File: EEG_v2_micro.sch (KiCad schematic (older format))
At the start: 19 parts, among them U6 CC2540, U7 2450BM15A0002E, X1 32-MHz, X2 32-MHz

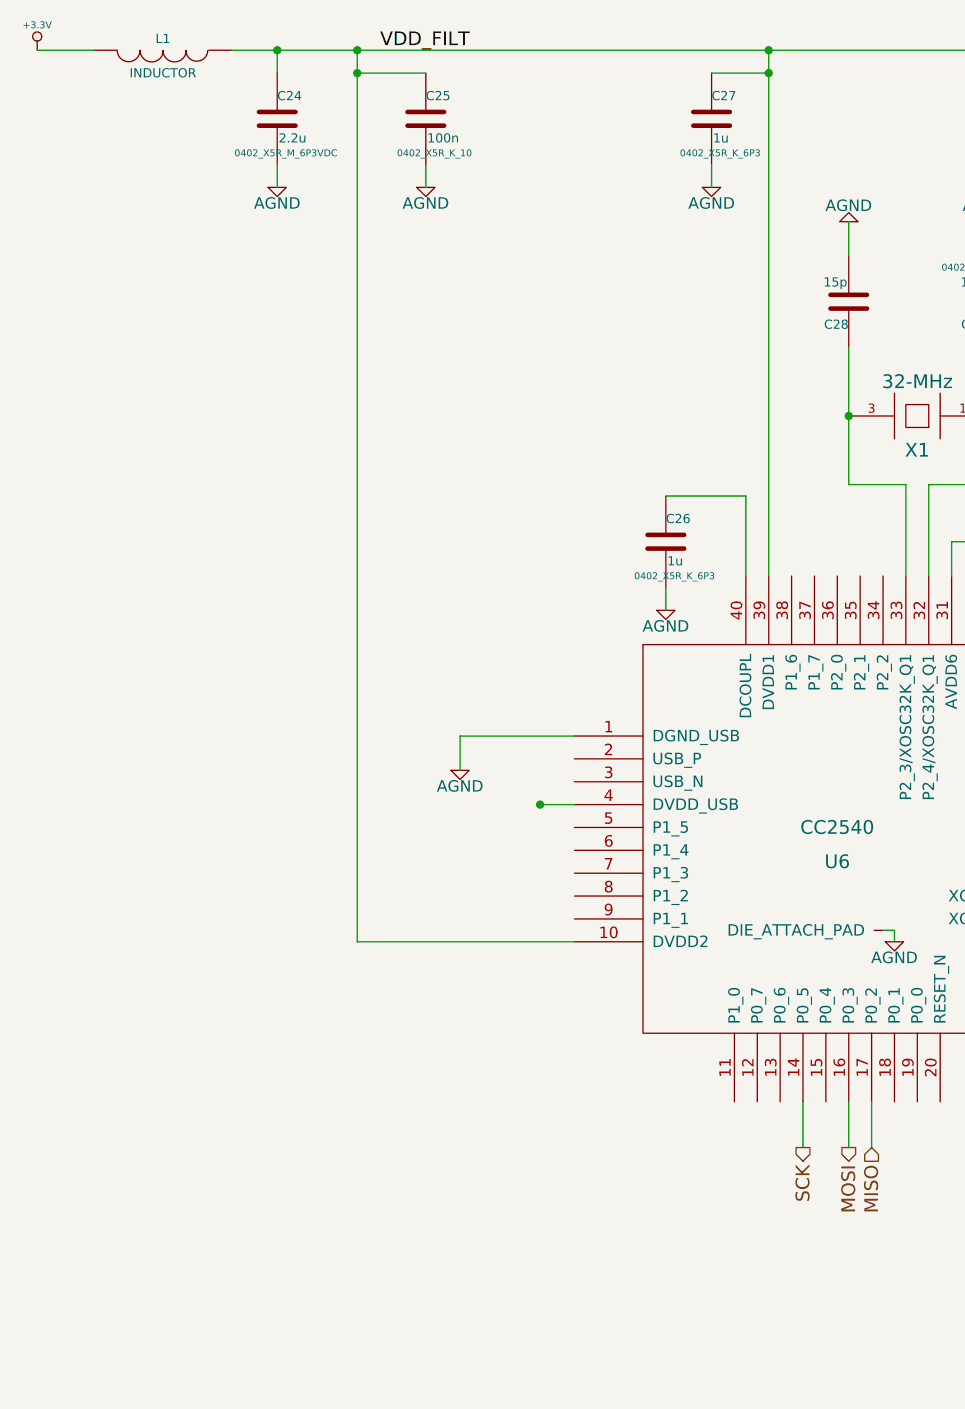
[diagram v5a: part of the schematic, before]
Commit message: Added USB connection.
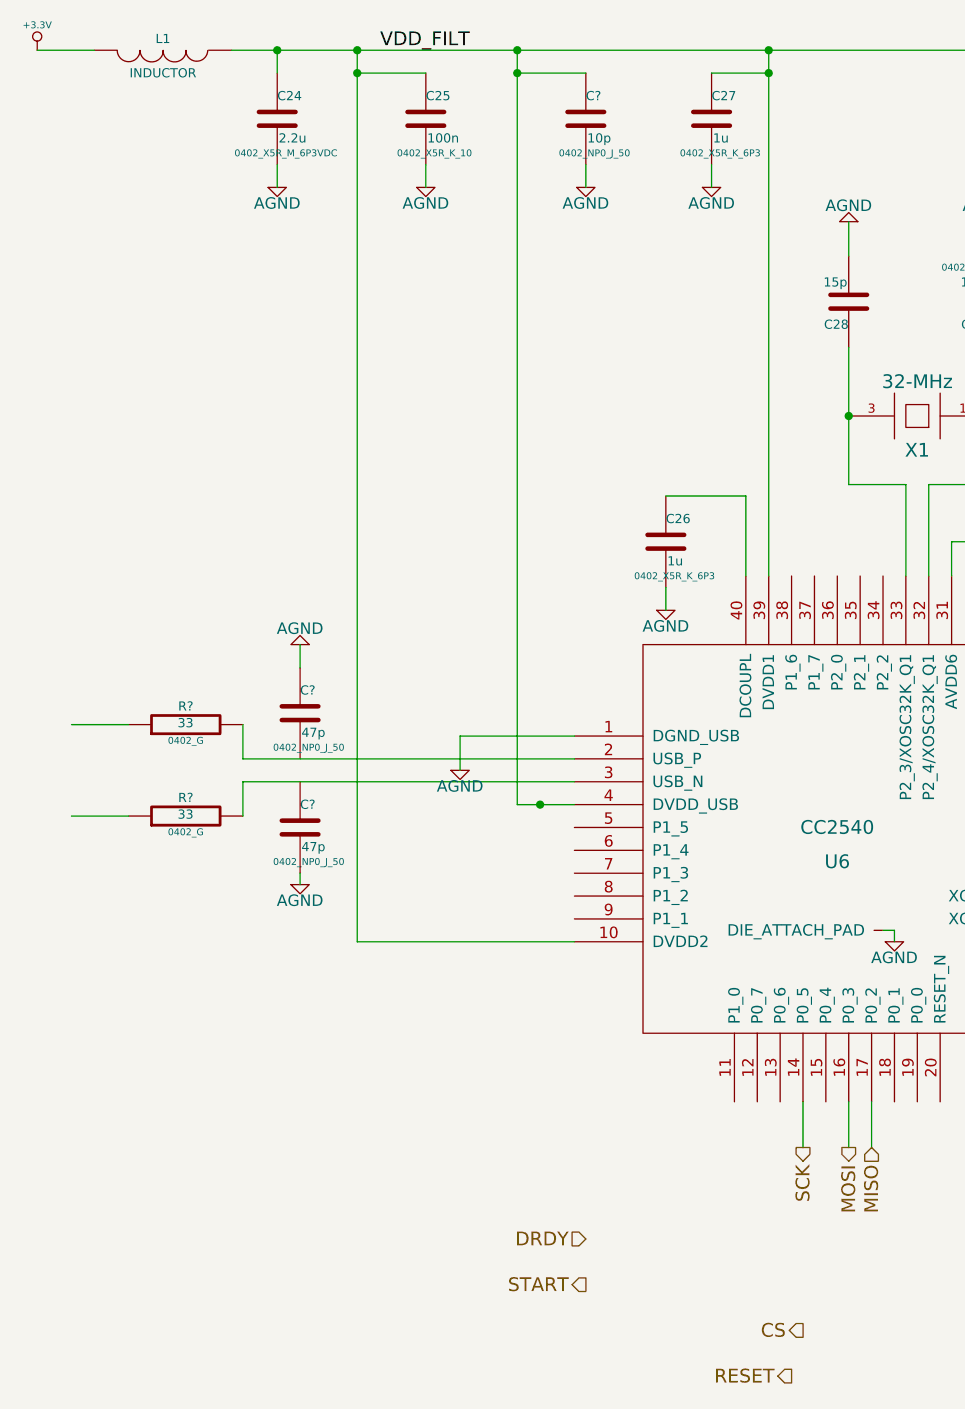
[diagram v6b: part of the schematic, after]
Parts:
- added C?: 10p, 0402_NP0_J_50, symbol C
- added C? (x2): 47p, 0402_NP0_J_50, symbol C
- added R? (x2): 33, 0402_G, symbol R
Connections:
- net labels added: CS, DRDY, RESET, START
- wire segments 71 -> 82
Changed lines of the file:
@@
 Sheet 4 4
 Title "Project Synapse Prototype Board"
-Date "14 jan 2015"
+Date "15 jan 2015"
 Rev "A.b"
 Comp "Senior Design 14-15"
@@
 	3850 1400 3850 3700
 Wire Wire Line
-	2850 4700 3000 4700
+	2750 4700 3000 4700
 Wire Wire Line
 	2050 5300 3000 5300
@@
 Text Notes 9550 4350 0    60   ~ 0
 Antenna (50 Ohm)
+Text HLabel 3050 6600 0    60   Input ~ 0
+DRDY
+Text HLabel 3050 6800 0    60   Output ~ 0
+START
+Text HLabel 4000 7000 0    60   Output ~ 0
+CS
+Text HLabel 3950 7200 0    60   Output ~ 0
+RESET
+$Comp
+L C C?
+U 1 1 54B75300
+P 3050 1700
+F 0 "C?" H 3050 1800 40  0000 L CNN
+F 1 "10p" H 3056 1615 40  0000 L CNN
+F 2 "0402_NP0_J_50" H 3088 1550 30  0000 C CNN
+F 3 "~" H 3050 1700 60  0000 C CNN
+	1    3050 1700
+	1    0    0    -1
+$EndComp
+$Comp
+L AGND #PWR?
+U 1 1 54B75306
+P 3050 2000
+F 0 "#PWR?" H 3050 2000 40  0001 C CNN
+F 1 "AGND" H 3050 1930 50  0000 C CNN
+F 2 "~" H 3050 2000 60  0000 C CNN
+F 3 "~" H 3050 2000 60  0000 C CNN
+	1    3050 2000
+	1    0    0    -1
+$EndComp
+Wire Wire Line
+	3050 1900 3050 2000
+Wire Wire Line
+	2750 4700 2750 1400
+Connection ~ 2750 1400
+Wire Wire Line
+	3050 1500 2750 1500
+Connection ~ 2750 1500
+Wire Wire Line
+	3000 4500 1550 4500
+Wire Wire Line
+	3000 4600 1550 4600
+$Comp
+L R R?
+U 1 1 54B7579A
+P 1300 4350
+F 0 "R?" V 1380 4350 40  0000 C CNN
+F 1 "33" V 1307 4351 40  0000 C CNN
+F 2 "0402_G" V 1230 4350 30  0000 C CNN
+F 3 "~" H 1300 4350 30  0000 C CNN
+	1    1300 4350
+	0    -1   -1   0
+$EndComp
+$Comp
+L R R?
+U 1 1 54B757A0
+P 1300 4750
+F 0 "R?" V 1380 4750 40  0000 C CNN
+F 1 "33" V 1307 4751 40  0000 C CNN
+F 2 "0402_G" V 1230 4750 30  0000 C CNN
+F 3 "~" H 1300 4750 30  0000 C CNN
+	1    1300 4750
+	0    -1   -1   0
+$EndComp
+Wire Wire Line
+	1550 4600 1550 4750
+Wire Wire Line
+	1550 4500 1550 4350
+Wire Wire Line
+	1050 4350 800  4350
+Wire Wire Line
+	1050 4750 800  4750
+$Comp
+L C C?
+U 1 1 54B75968
+P 1800 4800
+F 0 "C?" H 1800 4900 40  0000 L CNN
+F 1 "47p" H 1806 4715 40  0000 L CNN
+F 2 "0402_NP0_J_50" H 1838 4650 30  0000 C CNN
+F 3 "~" H 1800 4800 60  0000 C CNN
+	1    1800 4800
+	1    0    0    -1
+$EndComp
+$Comp
+L C C?
+U 1 1 54B75989
+P 1800 4300
+F 0 "C?" H 1800 4400 40  0000 L CNN
+F 1 "47p" H 1806 4215 40  0000 L CNN
+F 2 "0402_NP0_J_50" H 1838 4150 30  0000 C CNN
+F 3 "~" H 1800 4300 60  0000 C CNN
+	1    1800 4300
+	1    0    0    -1
+$EndComp
+$Comp
+L AGND #PWR?
+U 1 1 54B75999
+P 1800 5050
+F 0 "#PWR?" H 1800 5050 40  0001 C CNN
+F 1 "AGND" H 1800 4980 50  0000 C CNN
+F 2 "~" H 1800 5050 60  0000 C CNN
+F 3 "~" H 1800 5050 60  0000 C CNN
+	1    1800 5050
+	1    0    0    -1
+$EndComp
+$Comp
+L AGND #PWR?
+U 1 1 54B7599F
+P 1800 4000
+F 0 "#PWR?" H 1800 4000 40  0001 C CNN
+F 1 "AGND" H 1800 3930 50  0000 C CNN
+F 2 "~" H 1800 4000 60  0000 C CNN
+F 3 "~" H 1800 4000 60  0000 C CNN
+	1    1800 4000
+	-1   0    0    1
+$EndComp
+Wire Wire Line
+	1800 4000 1800 4100
+Wire Wire Line
+	1800 5000 1800 5050
 $EndSCHEMATC

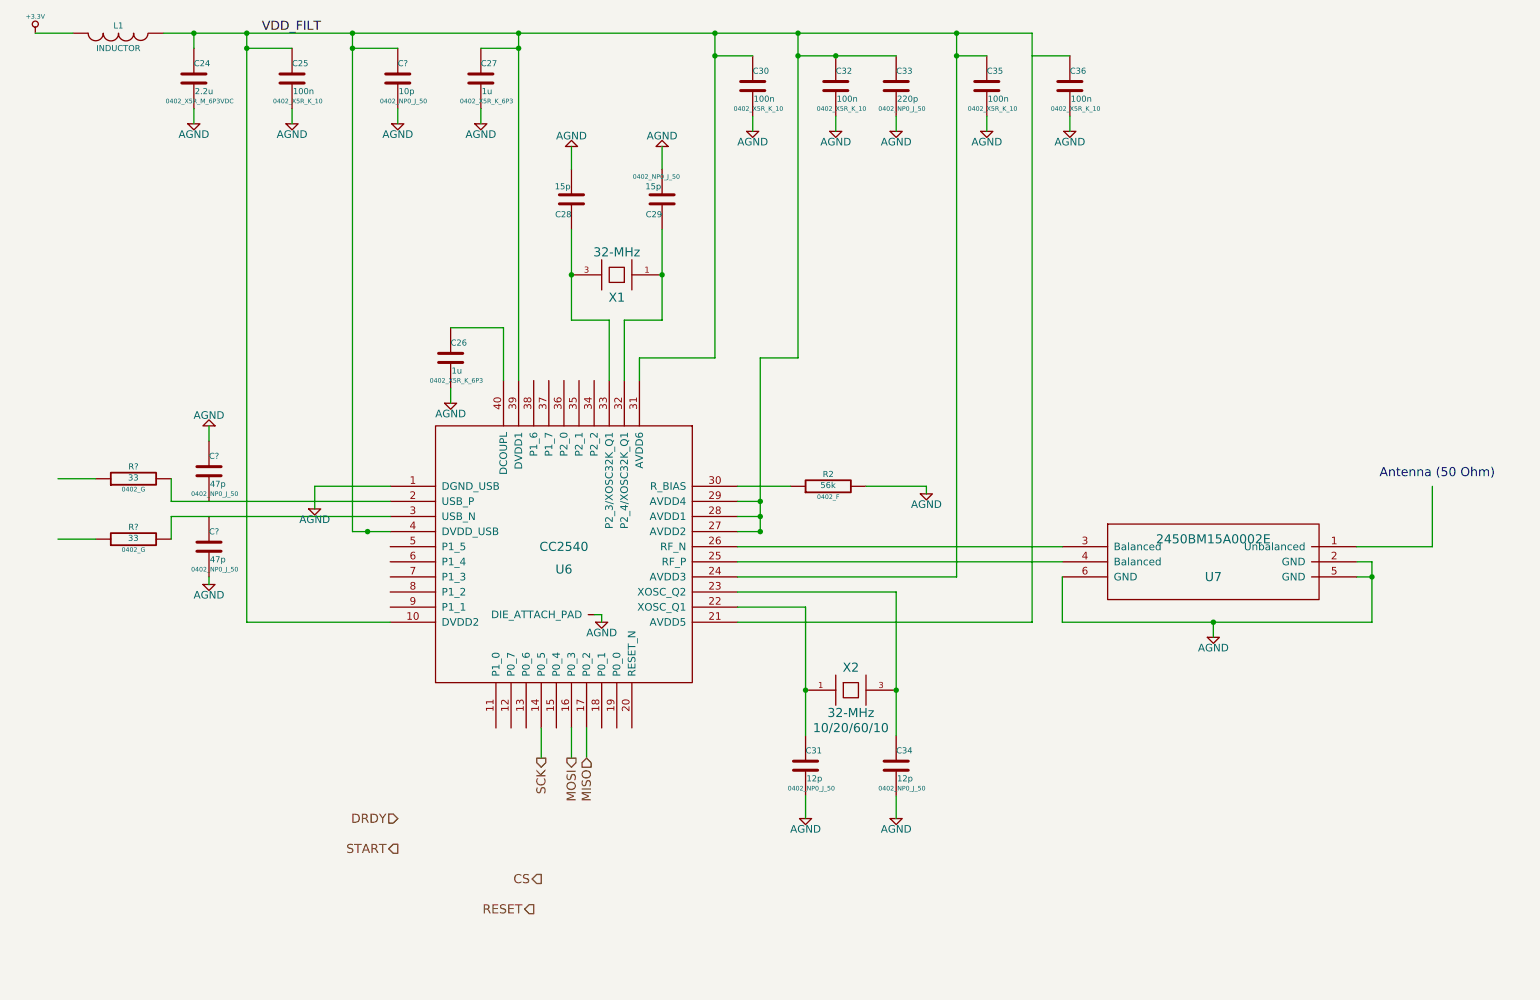
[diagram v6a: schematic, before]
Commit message: Microcontroller Sheet Work
Add antenna components and label. Add debug flash hier pins. Add RC
filter for RESET_N pin. Add heir labels for USB.
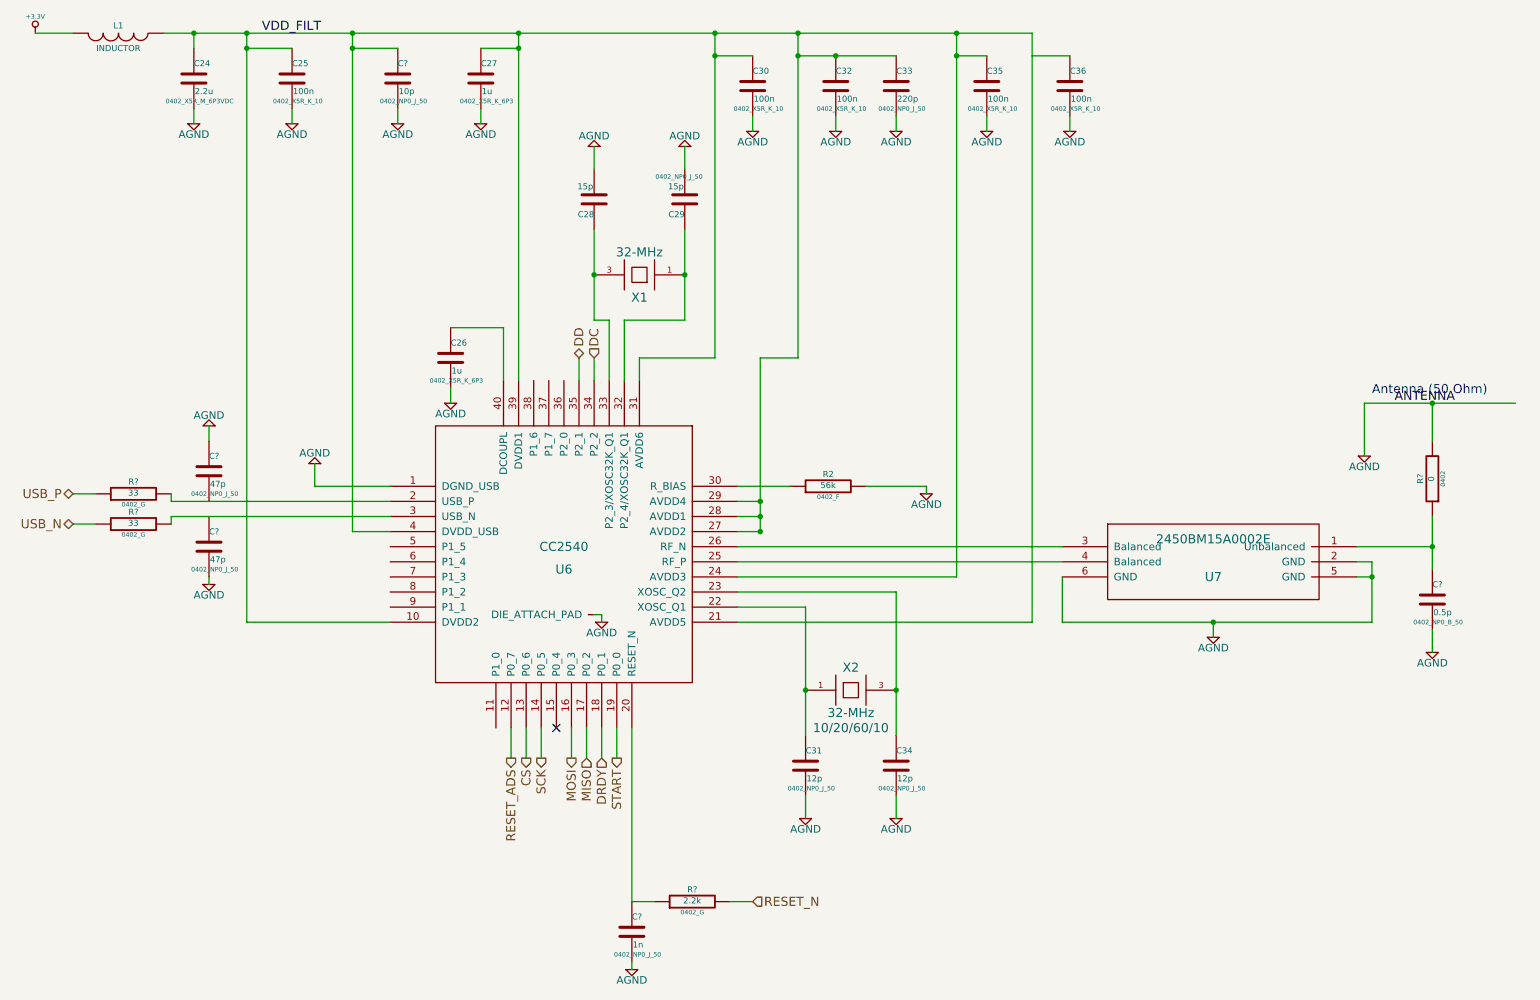
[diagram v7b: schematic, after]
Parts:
- added C?: 1n, 0402_NP0_J_50, symbol C
- added C?: 0.5p, 0402_NP0_B_50, symbol C
- added R?: 2.2k, 0402_G, symbol R
- added R?: 0, 0402, symbol R
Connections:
- net labels added: ANTENNA, DC, DD, RESET_ADS, RESET_N, USB_N, USB_P
- net labels removed: RESET
- wire segments 82 -> 96
- no-connect marks 0 -> 1
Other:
- moved on the sheet: C28, C29, R?, X1
